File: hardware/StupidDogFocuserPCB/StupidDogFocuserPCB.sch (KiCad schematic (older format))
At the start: 17 parts, among them M1 Stepper_Motor_bipolar, SW1 Rotary_Encoder_Switch, U1 DHT11, U2 SN74HC14N

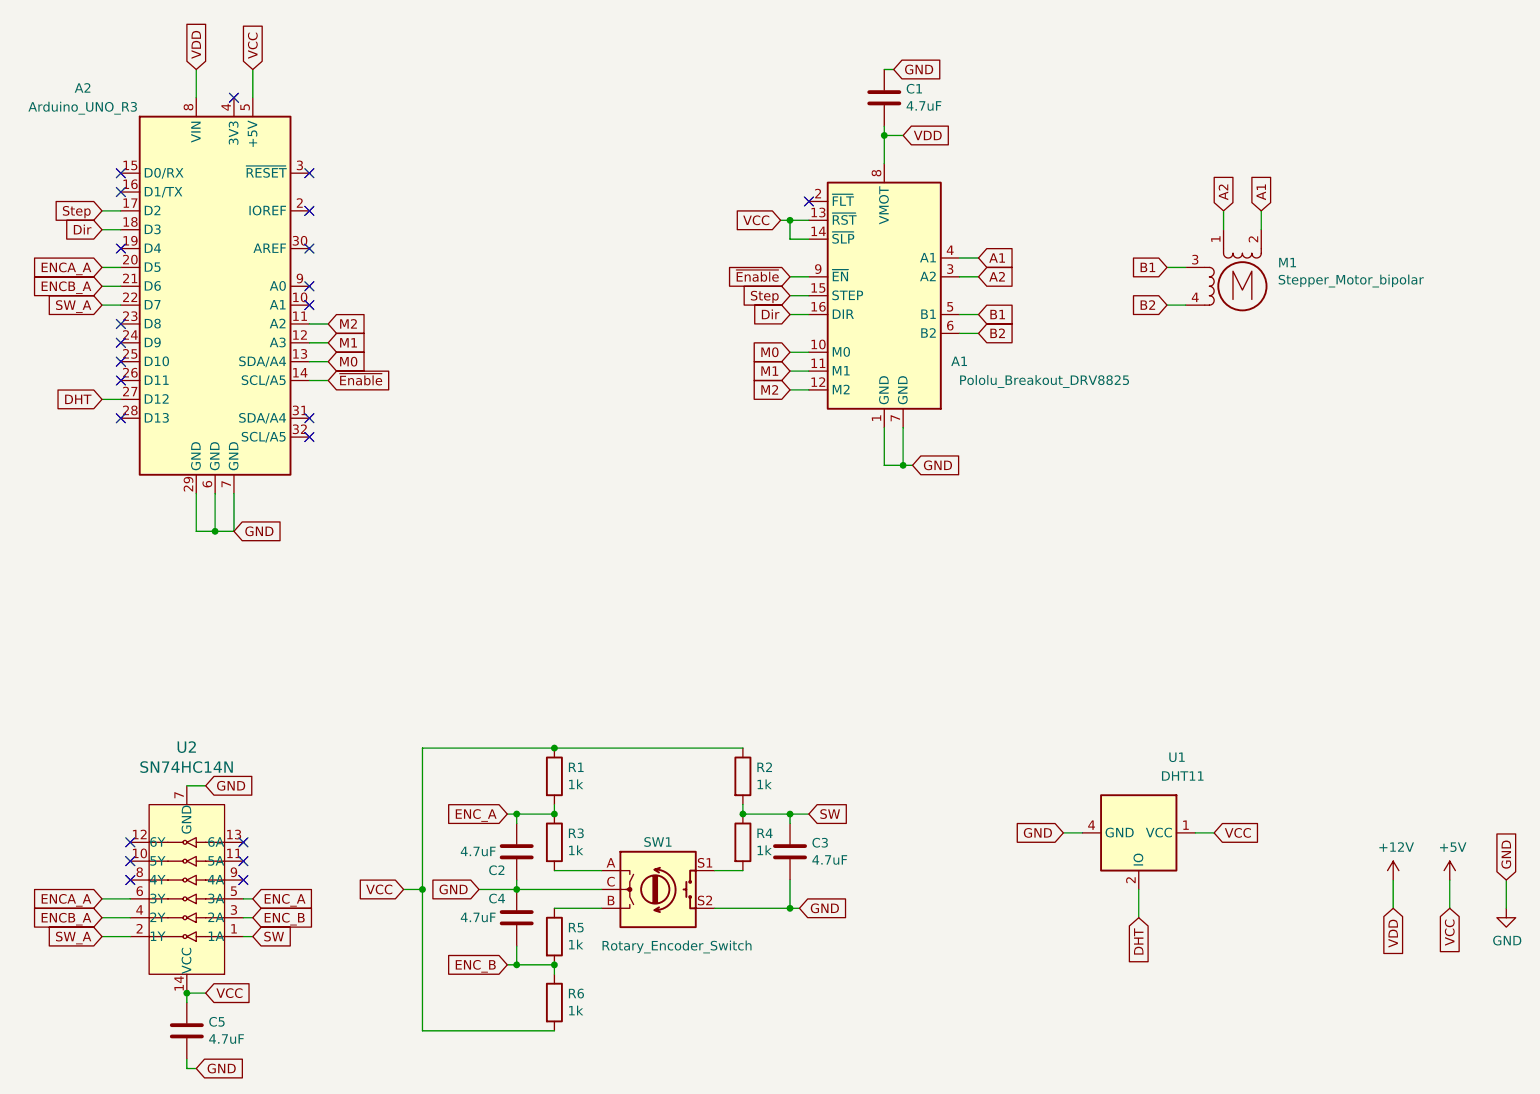
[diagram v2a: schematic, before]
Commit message: Hardware/bugs (#26)
* ASCOM6 Template

* ASCOM commands ported in from firmware

* remove readme.htm. Will replace with Readme.md when I get around to it.

* Updated schematic. Added limit switch. Moved encoder to the right and the stepper to the left. Adjusted resistor and capacitor sizes. Added screw terminals. Moved DHT11 to where it can bend out.

* thicker traces for the home gamer. Cleanup bends. Moved test points around.

* regenerate gerbers

* pcb

Co-authored-by: Jeff Voight <jeff.voight@gmail.com>
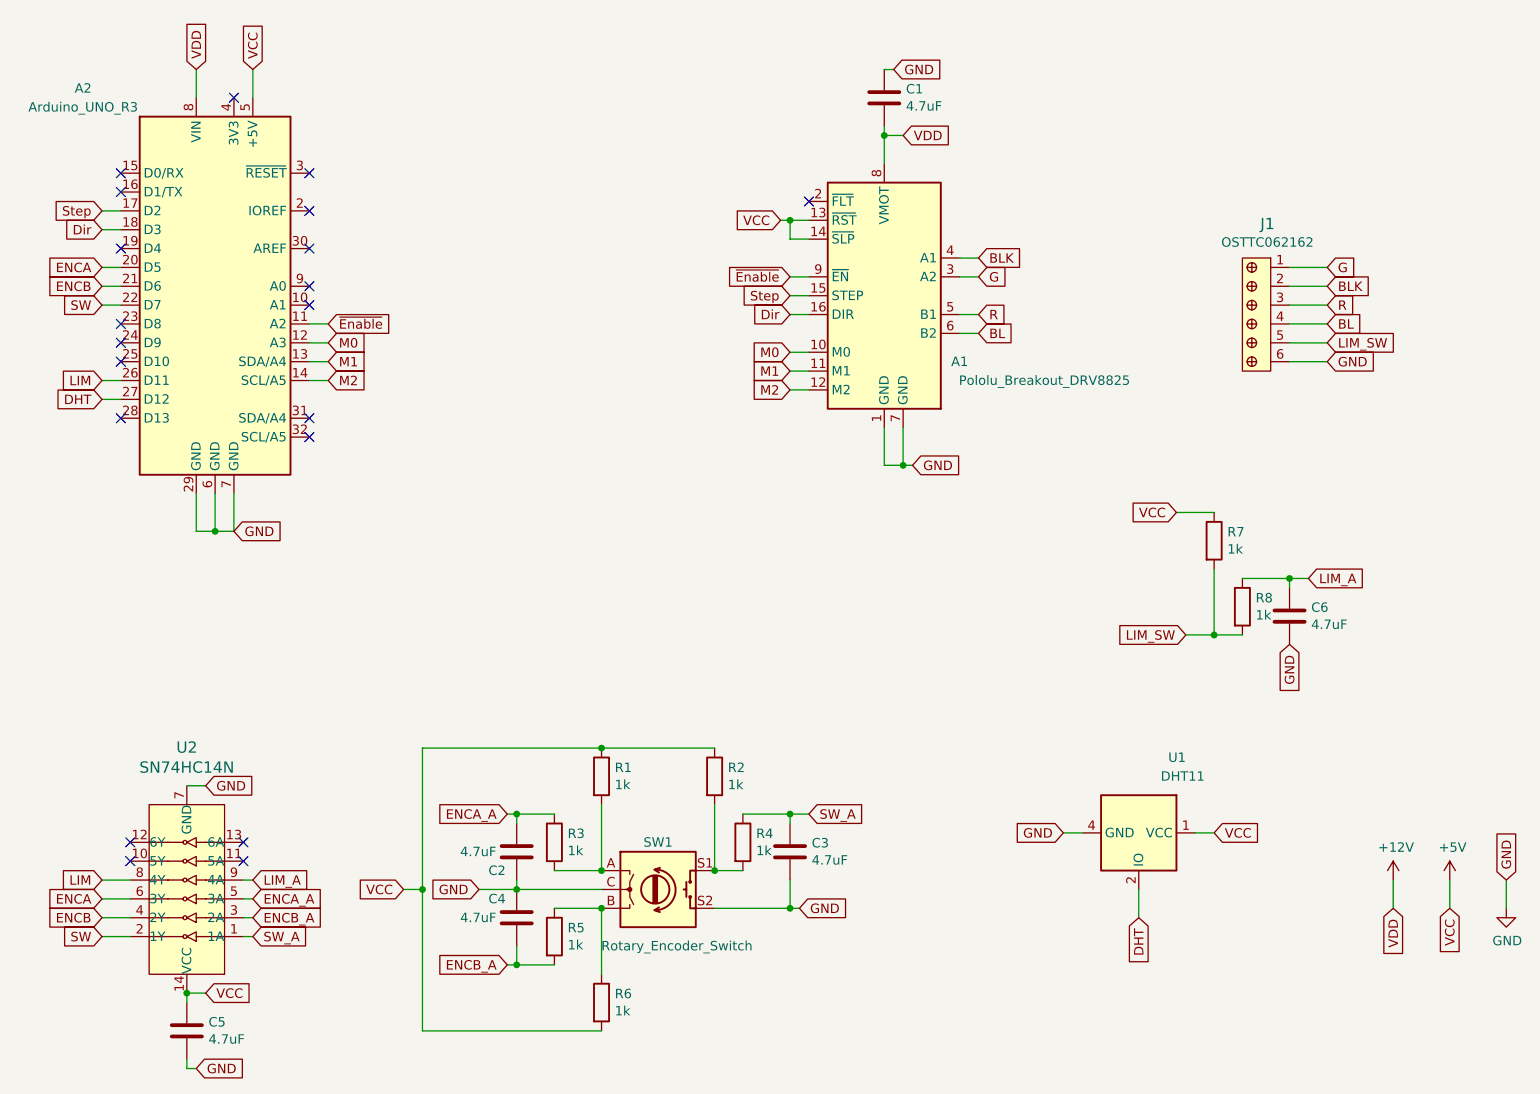
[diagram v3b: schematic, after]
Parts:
- removed M1: Stepper_Motor_bipolar, Connector_PinHeader_2.54mm:PinHeader_1x04_P2.54mm_Vertical, symbol Motor:Stepper_Motor_bipolar
- added C6: 4.7uF, Capacitor_THT:C_Disc_D3.0mm_W2.0mm_P2.50mm, symbol Device:C
- added J1: OSTTC062162, digikey-footprints:Term_Block_1x6_P5.08mm, symbol dk_Terminal-Blocks-Wire-to-Board:OSTTC062162
- added R7, R8: 1k, Resistor_THT:R_Axial_DIN0204_L3.6mm_D1.6mm_P7.62mm_Horizontal, symbol Device:R
- C1: footprint Capacitor_THT:C_Disc_D3.0mm_W2.0mm_P2.50mm -> Capacitor_THT:C_Disc_D4.7mm_W2.5mm_P5.00mm
- R1, R2, R3, R4, R5, R6: footprint Resistor_THT:R_Axial_DIN0204_L3.6mm_D1.6mm_P5.08mm_Horizontal -> Resistor_THT:R_Axial_DIN0204_L3.6mm_D1.6mm_P7.62mm_Horizontal
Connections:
- net +5V: now also R7.1
- net ENCA_A: now also C2.1, R3.1, U2.5 (3A); no longer A2.20 (D5), U2.6 (3Y)
- net ENCB_A: now also C4.2, R5.2, U2.3 (2A); no longer A2.21 (D6), U2.4 (2Y)
- net GND: now also C6.2, J1.6
- net M0: now also A2.12 (A3); no longer A2.13 (SDA/A4)
- net M1: now also A2.13 (SDA/A4); no longer A2.12 (A3)
- net M2: now also A2.14 (SCL/A5); no longer A2.11 (A2)
- net SW: now also A2.22 (D7), U2.2 (1Y); no longer C3.1, R2.2, R4.1, U2.1 (1A)
- net SW_A: now also C3.1, R4.1, U2.1 (1A); no longer A2.22 (D7), U2.2 (1Y)
- net ~Enable: now also A2.11 (A2); no longer A2.14 (SCL/A5)
- net LIM: now reaches A2.26 (D11)
- net LIM: now also U2.8 (4Y)
- net at R3.2, SW1.A: now also R1.2
- net at R5.1, SW1.B: now also R6.1
- net at R4.2, SW1.S1: now also R2.2
- net LIM_A: now reaches U2.9 (4A)
- net LIM_A: now also C6.1, R8.1
- net A1 renamed BLK
- net BLK: now also J1.2
- net A2 renamed G
- net G: now also J1.1
- net B1 renamed R
- net R: now also J1.3
- net B2 renamed BL
- net BL: now also J1.4
- removed net ENC_A: C2.1, R1.2, R3.1, U2.5 (3A)
- removed net ENC_B: C4.2, R5.2, R6.1, U2.3 (2A)
- new net ENCA: A2.20 (D5), U2.6 (3Y)
- new net ENCB: A2.21 (D6), U2.4 (2Y)
- new net LIM_SW: J1.5, R7.2, R8.2
- no-connect marks 23 -> 20
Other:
- moved on the sheet: R1, R2, R6
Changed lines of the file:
@@
 Wire Wire Line
 	6700 2200 6800 2200
-Wire Wire Line
-	7800 2450 7900 2450
-Wire Wire Line
-	7800 2250 7900 2250
-Wire Wire Line
-	8300 1950 8300 2050
-Wire Wire Line
-	8100 1950 8100 2050
-Text GLabel 8300 1950 1    50   Input ~ 0
-A1
-Text GLabel 8100 1950 1    50   Input ~ 0
-A2
-Text GLabel 7800 2450 0    50   Input ~ 0
-B2
-Text GLabel 7800 2250 0    50   Input ~ 0
-B1
+Text GLabel 8650 2250 2    50   Input ~ 0
+G
+Text GLabel 8650 2350 2    50   Input ~ 0
+BLK
+Text GLabel 8650 2550 2    50   Input ~ 0
+BL
+Text GLabel 8650 2450 2    50   Input ~ 0
+R
 Text GLabel 6800 2600 2    50   Input ~ 0
-B2
+BL
 Text GLabel 6800 2500 2    50   Input ~ 0
-B1
+R
 Text GLabel 6800 2300 2    50   Input ~ 0
-A2
+G
 Text GLabel 6800 2200 2    50   Input ~ 0
-A1
+BLK
 Wire Wire Line
 	5800 2700 5900 2700
@@
 Text GLabel 2150 2950 0    50   Input ~ 0
 DHT
-Text GLabel 3350 2750 2    50   Input ~ 0
+Text GLabel 3350 2650 2    50   Input ~ 0
 M0
 Text GLabel 2150 2450 0    50   Input ~ 0
-SW_A
+SW
 Text GLabel 2150 2350 0    50   Input ~ 0
-ENCB_A
+ENCB
 Text GLabel 2150 2250 0    50   Input ~ 0
-ENCA_A
-Text GLabel 3350 2850 2    50   Input ~ 0
+ENCA
+Text GLabel 3350 2550 2    50   Input ~ 0
 ~Enable
 Text GLabel 5800 2500 0    50   Input ~ 0
@@
 	2150 5600 2300 5600
 Text GLabel 2150 5600 0    50   Input ~ 0
-ENCA_A
+ENCA
 Text GLabel 2150 5700 0    50   Input ~ 0
-ENCB_A
+ENCB
 Text GLabel 2150 5800 0    50   Input ~ 0
-SW_A
+SW
 NoConn ~ 2300 5300
 NoConn ~ 2300 5400
-NoConn ~ 2300 5500
-NoConn ~ 2900 5500
 NoConn ~ 2900 5400
 NoConn ~ 2900 5300
@@
 	2900 5600 2950 5600
 Text GLabel 2950 5800 2    50   Input ~ 0
-SW
+SW_A
 Text GLabel 2950 5700 2    50   Input ~ 0
-ENC_B
+ENCB_A
 Text GLabel 2950 5600 2    50   Input ~ 0
-ENC_A
+ENCA_A
 Wire Wire Line
 	5400 5450 5550 5450
@@
 Wire Wire Line
 	5550 5150 5800 5150
-Connection ~ 5550 5150
 Text GLabel 5900 5150 2    50   Input ~ 0
-SW
-Wire Wire Line
-	5550 5100 5550 5150
-Connection ~ 4550 4800
-Wire Wire Line
-	5550 4800 4550 4800
+SW_A
+Connection ~ 4800 4800
+Wire Wire Line
+	5400 4800 4800 4800
 Connection ~ 3850 5550
 Wire Wire Line
-	3850 6300 4550 6300
+	3850 6300 4800 6300
 Wire Wire Line
 	3850 5550 3850 6300
 Wire Wire Line
-	3850 4800 4550 4800
+	3850 4800 4800 4800
 Wire Wire Line
 	3850 5550 3850 4800
@@
 Wire Wire Line
 	4300 5950 4350 5950
-Connection ~ 4550 5950
 Text GLabel 4300 5950 0    50   Input ~ 0
-ENC_B
-Connection ~ 4550 5150
+ENCB_A
 Text GLabel 4300 5150 0    50   Input ~ 0
-ENC_A
-Wire Wire Line
-	4550 5950 4550 6000
-Wire Wire Line
-	4550 5100 4550 5150
+ENCA_A
 Wire Wire Line
 	4550 5650 4800 5650
@@
 F 0 "C1" H 6415 1396 50  0000 L CNN
 F 1 "4.7uF" H 6415 1305 50  0000 L CNN
-F 2 "Capacitor_THT:C_Disc_D3.0mm_W2.0mm_P2.50mm" H 6338 1200 50  0001 C CNN
+F 2 "Capacitor_THT:C_Disc_D4.7mm_W2.5mm_P5.00mm" H 6338 1200 50  0001 C CNN
 F 3 "~" H 6300 1350 50  0001 C CNN
 	1    6300 1350
@@
 $EndComp
 $Comp
-L Motor:Stepper_Motor_bipolar M1
-U 1 1 5E4AD4CA
-P 8200 2350
-F 0 "M1" H 8388 2474 50  0000 L CNN
-F 1 "Stepper_Motor_bipolar" H 8388 2383 50  0000 L CNN
-F 2 "Connector_PinHeader_2.54mm:PinHeader_1x04_P2.54mm_Vertical" H 8210 2340 50  0001 C CNN
-F 3 "http://www.infineon.com/dgdl/Application-Note-TLE8110EE_driving_UniPolarStepperMotor_V1.1.pdf?fileId=db3a30431be39b97011be5d0aa0a00b0" H 8210 2340 50  0001 C CNN
-	1    8200 2350
-	1    0    0    -1
-$EndComp
-$Comp
 L Device:R R2
 U 1 1 5E4AB473
-P 5550 4950
-F 0 "R2" H 5620 4996 50  0000 L CNN
-F 1 "1k" H 5620 4905 50  0000 L CNN
-F 2 "Resistor_THT:R_Axial_DIN0204_L3.6mm_D1.6mm_P5.08mm_Horizontal" V 5480 4950 50  0001 C CNN
-F 3 "~" H 5550 4950 50  0001 C CNN
-	1    5550 4950
+P 5400 4950
+F 0 "R2" H 5470 4996 50  0000 L CNN
+F 1 "1k" H 5470 4905 50  0000 L CNN
+F 2 "Resistor_THT:R_Axial_DIN0204_L3.6mm_D1.6mm_P7.62mm_Horizontal" V 5330 4950 50  0001 C CNN
+F 3 "~" H 5400 4950 50  0001 C CNN
+	1    5400 4950
 	1    0    0    -1
 $EndComp
@@
 F 0 "R4" H 5620 5346 50  0000 L CNN
 F 1 "1k" H 5620 5255 50  0000 L CNN
-F 2 "Resistor_THT:R_Axial_DIN0204_L3.6mm_D1.6mm_P5.08mm_Horizontal" V 5480 5300 50  0001 C CNN
+F 2 "Resistor_THT:R_Axial_DIN0204_L3.6mm_D1.6mm_P7.62mm_Horizontal" V 5480 5300 50  0001 C CNN
 F 3 "~" H 5550 5300 50  0001 C CNN
 	1    5550 5300
@@
 L Device:R R6
 U 1 1 5E4AADCA
-P 4550 6150
-F 0 "R6" H 4620 6196 50  0000 L CNN
-F 1 "1k" H 4620 6105 50  0000 L CNN
-F 2 "Resistor_THT:R_Axial_DIN0204_L3.6mm_D1.6mm_P5.08mm_Horizontal" V 4480 6150 50  0001 C CNN
-F 3 "~" H 4550 6150 50  0001 C CNN
-	1    4550 6150
+P 4800 6150
+F 0 "R6" H 4870 6196 50  0000 L CNN
+F 1 "1k" H 4870 6105 50  0000 L CNN
+F 2 "Resistor_THT:R_Axial_DIN0204_L3.6mm_D1.6mm_P7.62mm_Horizontal" V 4730 6150 50  0001 C CNN
+F 3 "~" H 4800 6150 50  0001 C CNN
+	1    4800 6150
 	1    0    0    -1
 $EndComp
@@
 F 0 "R5" H 4620 5846 50  0000 L CNN
 F 1 "1k" H 4620 5755 50  0000 L CNN
-F 2 "Resistor_THT:R_Axial_DIN0204_L3.6mm_D1.6mm_P5.08mm_Horizontal" V 4480 5800 50  0001 C CNN
+F 2 "Resistor_THT:R_Axial_DIN0204_L3.6mm_D1.6mm_P7.62mm_Horizontal" V 4480 5800 50  0001 C CNN
 F 3 "~" H 4550 5800 50  0001 C CNN
 	1    4550 5800
@@
 F 0 "R3" H 4620 5346 50  0000 L CNN
 F 1 "1k" H 4620 5255 50  0000 L CNN
-F 2 "Resistor_THT:R_Axial_DIN0204_L3.6mm_D1.6mm_P5.08mm_Horizontal" V 4480 5300 50  0001 C CNN
+F 2 "Resistor_THT:R_Axial_DIN0204_L3.6mm_D1.6mm_P7.62mm_Horizontal" V 4480 5300 50  0001 C CNN
 F 3 "~" H 4550 5300 50  0001 C CNN
 	1    4550 5300
@@
 L Device:R R1
 U 1 1 5E4A9F5B
-P 4550 4950
-F 0 "R1" H 4620 4996 50  0000 L CNN
-F 1 "1k" H 4620 4905 50  0000 L CNN
-F 2 "Resistor_THT:R_Axial_DIN0204_L3.6mm_D1.6mm_P5.08mm_Horizontal" V 4480 4950 50  0001 C CNN
-F 3 "~" H 4550 4950 50  0001 C CNN
-	1    4550 4950
+P 4800 4950
+F 0 "R1" H 4870 4996 50  0000 L CNN
+F 1 "1k" H 4870 4905 50  0000 L CNN
+F 2 "Resistor_THT:R_Axial_DIN0204_L3.6mm_D1.6mm_P7.62mm_Horizontal" V 4730 4950 50  0001 C CNN
+F 3 "~" H 4800 4950 50  0001 C CNN
+	1    4800 4950
 	1    0    0    -1
 $EndComp
@@
 NoConn ~ 3250 3050
 NoConn ~ 3250 3150
-NoConn ~ 2250 2850
 NoConn ~ 2250 2750
 NoConn ~ 2250 2650
@@
 Text GLabel 5800 2900 0    50   Input ~ 0
 M2
-Text GLabel 3350 2650 2    50   Input ~ 0
+Text GLabel 3350 2750 2    50   Input ~ 0
 M1
-Text GLabel 3350 2550 2    50   Input ~ 0
+Text GLabel 3350 2850 2    50   Input ~ 0
 M2
 Wire Wire Line
@@
 Wire Wire Line
 	5900 2900 5800 2900
+Wire Wire Line
+	4800 5100 4800 5450
+Connection ~ 4800 5450
+Wire Wire Line
+	4800 6000 4800 5650
+Connection ~ 4800 5650
+Wire Wire Line
+	5400 5100 5400 5450
+Connection ~ 5400 5450
+Text GLabel 2150 2850 0    50   Input ~ 0
+LIM
+Wire Wire Line
+	2150 2850 2250 2850
+Text GLabel 2150 5500 0    50   Input ~ 0
+LIM
+Wire Wire Line
+	2150 5500 2300 5500
+Text GLabel 2950 5500 2    50   Input ~ 0
+LIM_A
+Wire Wire Line
+	2900 5500 2950 5500
+$Comp
+L dk_Terminal-Blocks-Wire-to-Board:OSTTC062162 J1
+U 1 1 5E624889
+P 8350 2250
+F 0 "J1" V 8119 2233 60  0000 C CNN
+F 1 "OSTTC062162" V 8217 2233 50  0000 C CNN
+F 2 "digikey-footprints:Term_Block_1x6_P5.08mm" H 8550 2450 60  0001 L CNN
+F 3 "http://www.on-shore.com/wp-content/uploads/OSTTCXX2162.pdf" H 8550 2550 60  0001 L CNN
+F 4 "ED2611-ND" H 8550 2650 60  0001 L CNN "Digi-Key_PN"
+F 5 "OSTTC042162" H 8550 2750 60  0001 L CNN "MPN"
+F 6 "Connectors, Interconnects" H 8550 2850 60  0001 L CNN "Category"
+F 7 "Terminal Blocks - Wire to Board" H 8550 2950 60  0001 L CNN "Family"
+F 8 "http://www.on-shore.com/wp-content/uploads/OSTTCXX2162.pdf" H 8550 3050 60  0001 L CNN "DK_Datasheet_Link"
+F 9 "/product-detail/en/on-shore-technology-inc/OSTTC042162/ED2611-ND/614560" H 8550 3150 60  0001 L CNN "DK_Detail_Page"
+F 10 "TERM BLK 4P SIDE ENT 5.08MM PCB" H 8550 3250 60  0001 L CNN "Description"
+F 11 "On Shore Technology Inc." H 8550 3350 60  0001 L CNN "Manufacturer"
+F 12 "Active" H 8550 3450 60  0001 L CNN "Status"
+	1    8350 2250
+	0    1    1    0
+$EndComp
+Wire Wire Line
+	8450 2250 8650 2250
+Wire Wire Line
+	8450 2350 8650 2350
+Wire Wire Line
+	8450 2450 8650 2450
+Wire Wire Line
+	8450 2550 8650 2550
+Text GLabel 8650 2650 2    50   Input ~ 0
+LIM_SW
+Text GLabel 8650 2750 2    50   Input ~ 0
+GND
+Wire Wire Line
+	8450 2650 8650 2650
+Wire Wire Line
+	8450 2750 8650 2750
+Wire Wire Line
+	8050 4200 8200 4200
+Wire Wire Line
+	8450 3900 8550 3900
+Connection ~ 8450 3900
+Wire Wire Line
+	8450 3950 8450 3900
+Wire Wire Line
+	8200 3900 8450 3900
+Text GLabel 8550 3900 2    50   Input ~ 0
+LIM_A
+Wire Wire Line
+	8050 3550 7850 3550
+$Comp
+L Device:R R7
+U 1 1 5E63E909
+P 8050 3700
+F 0 "R7" H 8120 3746 50  0000 L CNN
+F 1 "1k" H 8120 3655 50  0000 L CNN
+F 2 "Resistor_THT:R_Axial_DIN0204_L3.6mm_D1.6mm_P7.62mm_Horizontal" V 7980 3700 50  0001 C CNN
+F 3 "~" H 8050 3700 50  0001 C CNN
+	1    8050 3700
+	1    0    0    -1
+$EndComp
+$Comp
+L Device:R R8
+U 1 1 5E63E913
+P 8200 4050
+F 0 "R8" H 8270 4096 50  0000 L CNN
+F 1 "1k" H 8270 4005 50  0000 L CNN
+F 2 "Resistor_THT:R_Axial_DIN0204_L3.6mm_D1.6mm_P7.62mm_Horizontal" V 8130 4050 50  0001 C CNN
+F 3 "~" H 8200 4050 50  0001 C CNN
+	1    8200 4050
+	1    0    0    -1
+$EndComp
+$Comp
+L Device:C C6
+U 1 1 5E63E91D
+P 8450 4100
+F 0 "C6" H 8565 4146 50  0000 L CNN
+F 1 "4.7uF" H 8565 4055 50  0000 L CNN
+F 2 "Capacitor_THT:C_Disc_D3.0mm_W2.0mm_P2.50mm" H 8488 3950 50  0001 C CNN
+F 3 "~" H 8450 4100 50  0001 C CNN
+	1    8450 4100
+	1    0    0    -1
+$EndComp
+Wire Wire Line
+	8050 3850 8050 4200
+Text GLabel 7900 4200 0    50   Input ~ 0
+LIM_SW
+Wire Wire Line
+	7900 4200 8050 4200
+Connection ~ 8050 4200
+Text GLabel 7850 3550 0    50   Input ~ 0
+VCC
+Text GLabel 8450 4250 3    50   Input ~ 0
+GND
 $EndSCHEMATC

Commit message: Feature/pcbready (#30)
* cache update kicad?

* added temperature read back in

* minor tweaks to the code now that the PCB works.

* update indi driver to reflect changes. Remove microstep.

* speed read

Co-authored-by: Jeff Voight <jeff.voight@gmail.com>
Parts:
- J1: symbol dk_Terminal-Blocks-Wire-to-Board:OSTTC062162 -> StupidDogFocuserPCB-rescue:OSTTC062162-dk_Terminal-Blocks-Wire-to-Board
- U2: symbol dk_Logic-Gates-and-Inverters:SN74HC14N -> StupidDogFocuserPCB-rescue:SN74HC14N-dk_Logic-Gates-and-Inverters
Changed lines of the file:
@@
 $EndComp
 $Comp
-L dk_Logic-Gates-and-Inverters:SN74HC14N U2
+L StupidDogFocuserPCB-rescue:SN74HC14N-dk_Logic-Gates-and-Inverters U2
 U 1 1 5E4A594F
 P 2600 5500
@@
 	2900 5500 2950 5500
 $Comp
-L dk_Terminal-Blocks-Wire-to-Board:OSTTC062162 J1
+L StupidDogFocuserPCB-rescue:OSTTC062162-dk_Terminal-Blocks-Wire-to-Board J1
 U 1 1 5E624889
 P 8350 2250

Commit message: Feature/bompcbpads (#31)
* bill of materials

* added ground clip pad. Updated capacitor sizes. Regenerated gerbers.

Co-authored-by: Jeff Voight <jeff.voight@gmail.com>
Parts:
- C2, C3, C4, C5, C6: footprint Capacitor_THT:C_Disc_D3.0mm_W2.0mm_P2.50mm -> Capacitor_THT:C_Disc_D4.7mm_W2.5mm_P5.00mm
- J1: symbol StupidDogFocuserPCB-rescue:OSTTC062162-dk_Terminal-Blocks-Wire-to-Board -> StupidDogFocuserPCB-rescue:OSTTC062162-dk_Terminal-Blocks-Wire-to-Board-StupidDogFocuserPCB-rescue
- U2: symbol StupidDogFocuserPCB-rescue:SN74HC14N-dk_Logic-Gates-and-Inverters -> StupidDogFocuserPCB-rescue:SN74HC14N-dk_Logic-Gates-and-Inverters-StupidDogFocuserPCB-rescue
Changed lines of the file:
@@
 F 0 "C5" H 2715 6346 50  0000 L CNN
 F 1 "4.7uF" H 2715 6255 50  0000 L CNN
-F 2 "Capacitor_THT:C_Disc_D3.0mm_W2.0mm_P2.50mm" H 2638 6150 50  0001 C CNN
+F 2 "Capacitor_THT:C_Disc_D4.7mm_W2.5mm_P5.00mm" H 2638 6150 50  0001 C CNN
 F 3 "~" H 2600 6300 50  0001 C CNN
 	1    2600 6300
@@
 F 0 "C3" H 5915 5396 50  0000 L CNN
 F 1 "4.7uF" H 5915 5305 50  0000 L CNN
-F 2 "Capacitor_THT:C_Disc_D3.0mm_W2.0mm_P2.50mm" H 5838 5200 50  0001 C CNN
+F 2 "Capacitor_THT:C_Disc_D4.7mm_W2.5mm_P5.00mm" H 5838 5200 50  0001 C CNN
 F 3 "~" H 5800 5350 50  0001 C CNN
 	1    5800 5350
@@
 F 0 "C4" H 4200 5800 50  0000 L CNN
 F 1 "4.7uF" H 4050 5700 50  0000 L CNN
-F 2 "Capacitor_THT:C_Disc_D3.0mm_W2.0mm_P2.50mm" H 4388 5550 50  0001 C CNN
+F 2 "Capacitor_THT:C_Disc_D4.7mm_W2.5mm_P5.00mm" H 4388 5550 50  0001 C CNN
 F 3 "~" H 4350 5700 50  0001 C CNN
 	1    4350 5700
@@
 F 0 "C2" H 4200 5250 50  0000 L CNN
 F 1 "4.7uF" H 4050 5350 50  0000 L CNN
-F 2 "Capacitor_THT:C_Disc_D3.0mm_W2.0mm_P2.50mm" H 4388 5200 50  0001 C CNN
+F 2 "Capacitor_THT:C_Disc_D4.7mm_W2.5mm_P5.00mm" H 4388 5200 50  0001 C CNN
 F 3 "~" H 4350 5350 50  0001 C CNN
 	1    4350 5350
@@
 $EndComp
 $Comp
-L StupidDogFocuserPCB-rescue:SN74HC14N-dk_Logic-Gates-and-Inverters U2
+L StupidDogFocuserPCB-rescue:SN74HC14N-dk_Logic-Gates-and-Inverters-StupidDogFocuserPCB-rescue U2
 U 1 1 5E4A594F
 P 2600 5500
@@
 	2900 5500 2950 5500
 $Comp
-L StupidDogFocuserPCB-rescue:OSTTC062162-dk_Terminal-Blocks-Wire-to-Board J1
+L StupidDogFocuserPCB-rescue:OSTTC062162-dk_Terminal-Blocks-Wire-to-Board-StupidDogFocuserPCB-rescue J1
 U 1 1 5E624889
 P 8350 2250
@@
 F 0 "C6" H 8565 4146 50  0000 L CNN
 F 1 "4.7uF" H 8565 4055 50  0000 L CNN
-F 2 "Capacitor_THT:C_Disc_D3.0mm_W2.0mm_P2.50mm" H 8488 3950 50  0001 C CNN
+F 2 "Capacitor_THT:C_Disc_D4.7mm_W2.5mm_P5.00mm" H 8488 3950 50  0001 C CNN
 F 3 "~" H 8450 4100 50  0001 C CNN
 	1    8450 4100
